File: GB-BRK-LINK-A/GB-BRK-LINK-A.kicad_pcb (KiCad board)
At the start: 2 copper layers, 30 x 35 mm, 6 parts, among them J1 Conn_01x06, J2 GameBoy_LinkPort

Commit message: Adjust solder mask clearances, regenerate gerbers
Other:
- rule pad_to_mask_clearance: 0.051 -> 0
- rule solder_mask_min_width: 0.25 -> 0.2
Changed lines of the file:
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@@
     (pad_size 1.524 1.524)
     (pad_drill 0.762)
-    (pad_to_mask_clearance 0.051)
-    (solder_mask_min_width 0.25)
+    (pad_to_mask_clearance 0)
+    (solder_mask_min_width 0.2)
     (aux_axis_origin 0 0)
     (visible_elements FFFFFF7F)

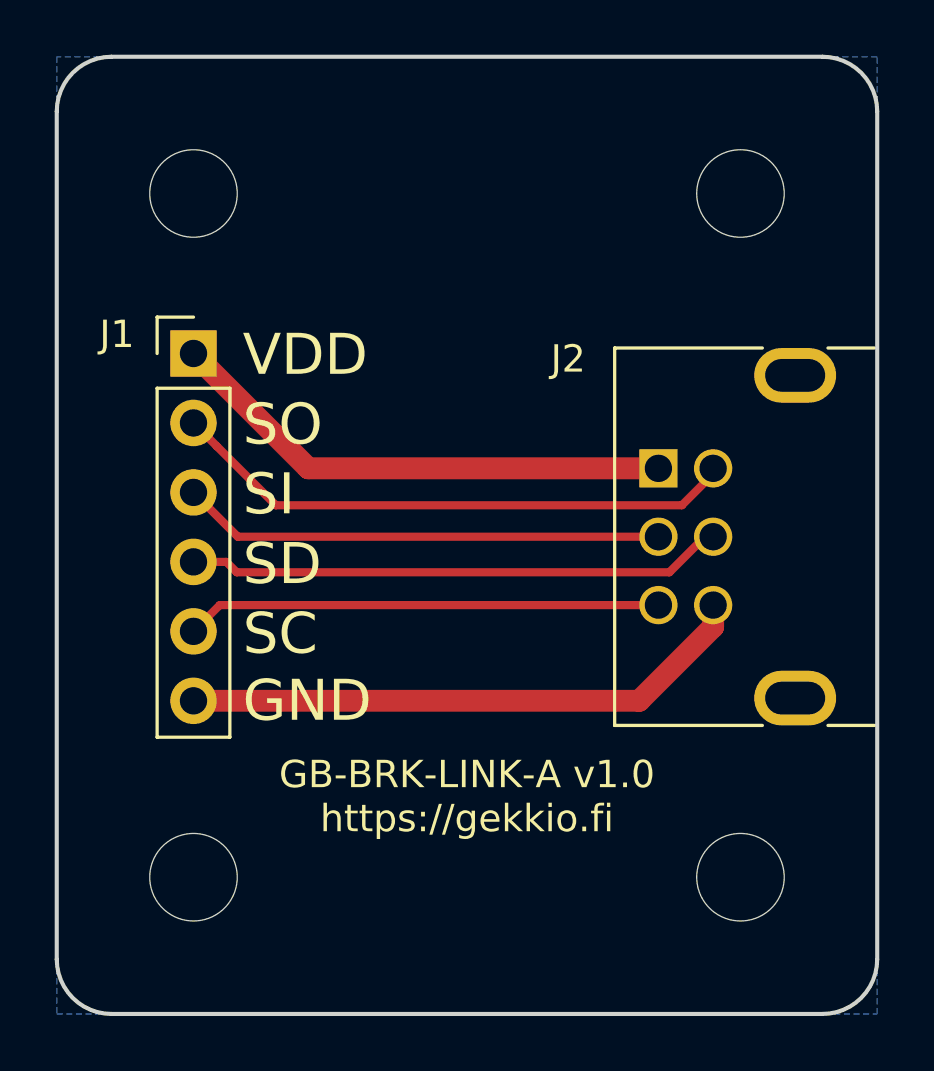
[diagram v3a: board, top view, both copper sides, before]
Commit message: Upgrade most projects to KiCad 6
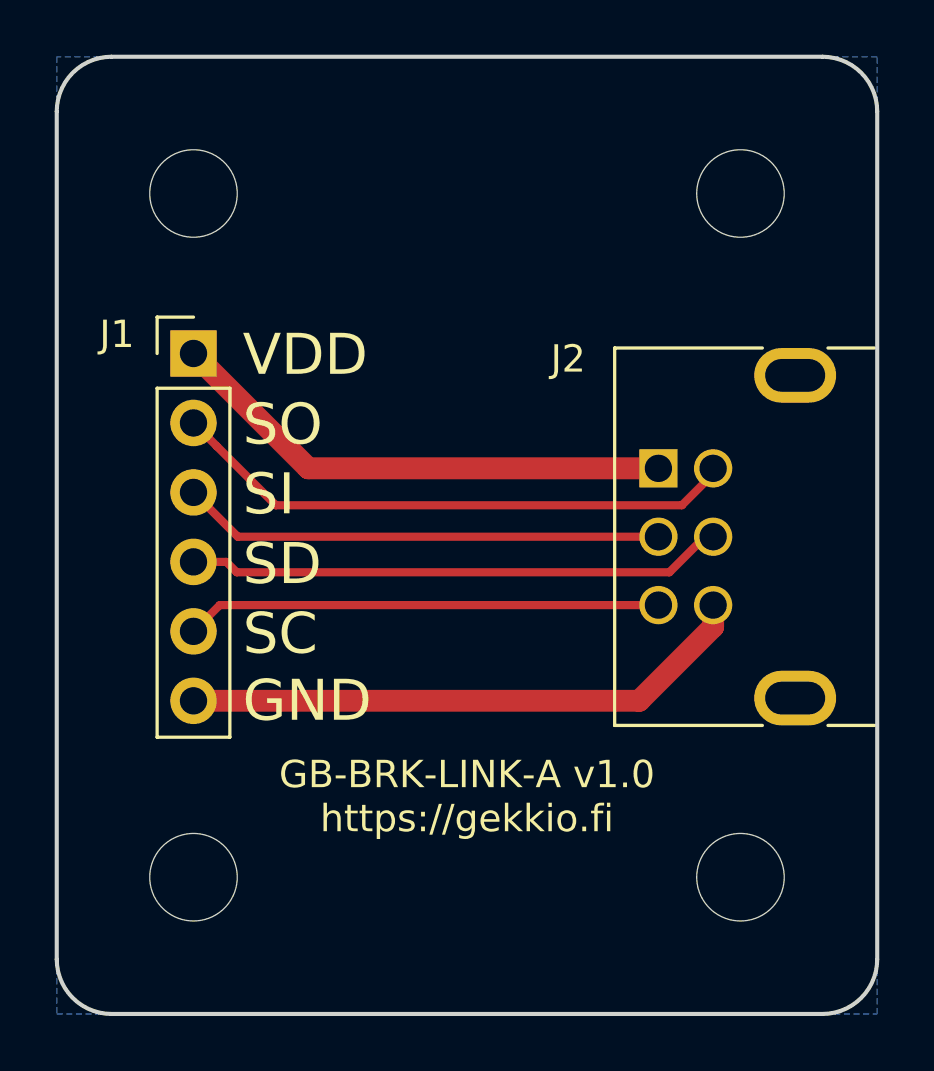
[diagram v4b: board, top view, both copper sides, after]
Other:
- net class Default removed
